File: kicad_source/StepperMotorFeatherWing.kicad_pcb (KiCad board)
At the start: 2 copper layers, 100 x 60 mm, 118 parts, among them CN1 ADAFRUIT_FEATHER, CN10 691322310004, CN11 BM05B-SRSS-TB, CN2 DNI, CN20 691322310004, CN21 BM05B-SRSS-TB, CN3 BM04B-SRSS-TB, CN4 CONN_01X04, CN5 691322310002, CN6 691313710002, Q1 IPD90P03P4L- 04, U1 TMC5130A-TA, U2 TMC5130A-TA, U3 LM1085ISX-ADJ/NOPB, U4 LM75BD, U9 IFX91041EJV, Y1 ECS-3225MV-160-BN-TR

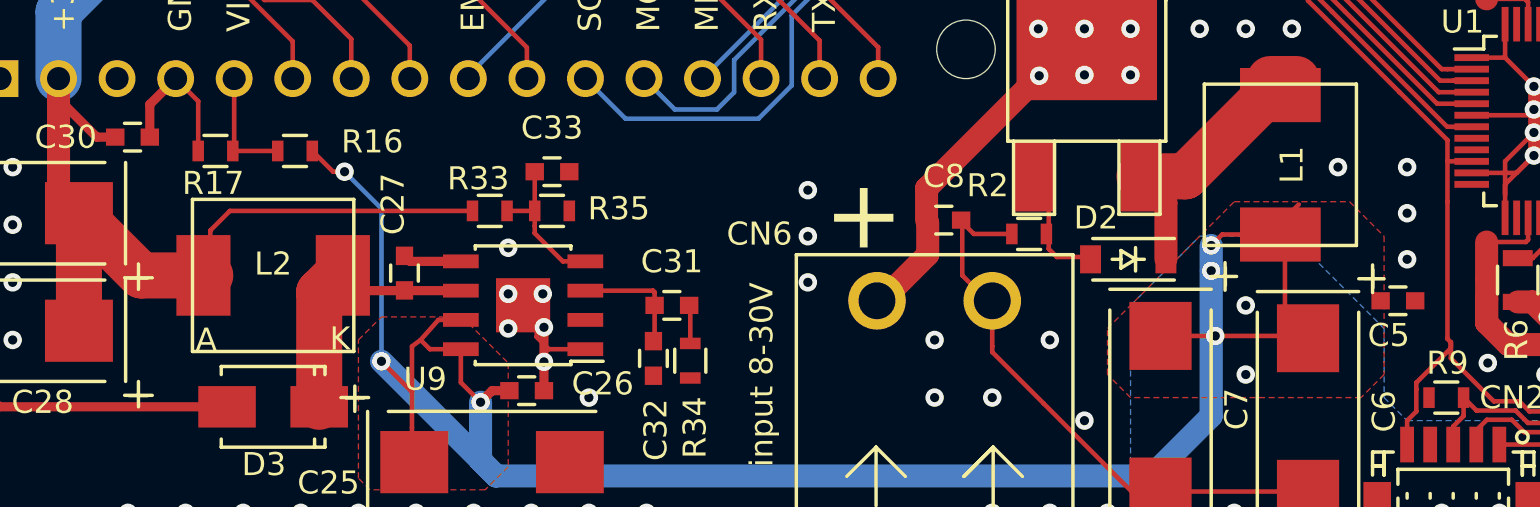
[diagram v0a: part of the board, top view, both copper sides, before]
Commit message: corrected order numbers of capacitors
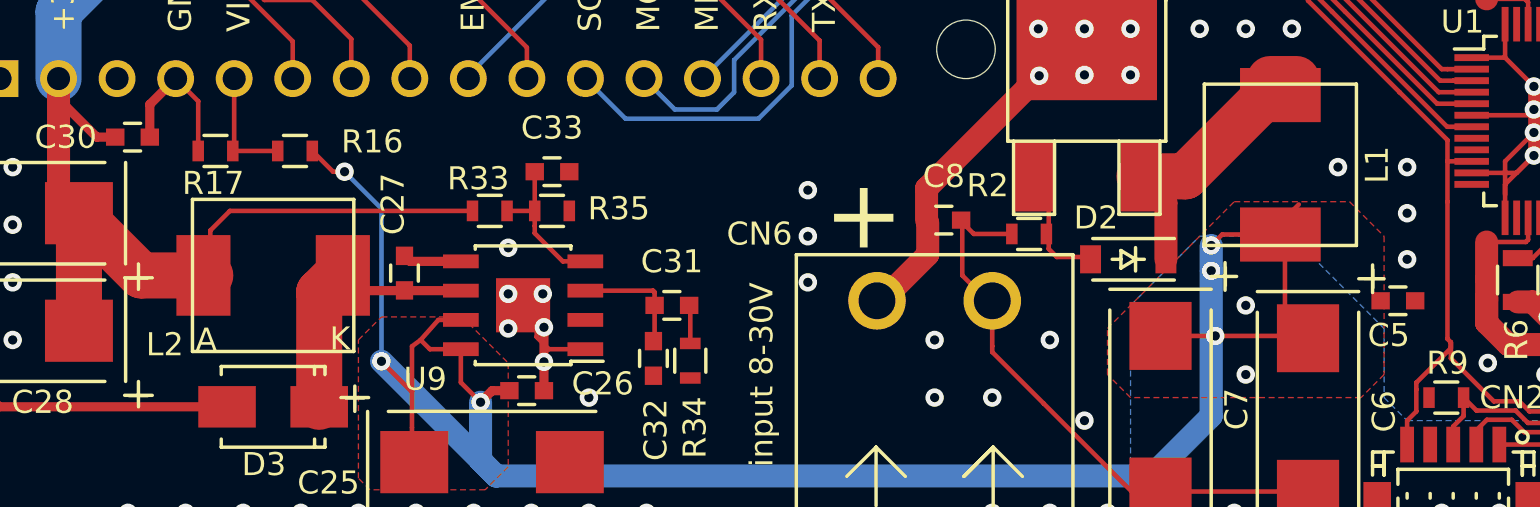
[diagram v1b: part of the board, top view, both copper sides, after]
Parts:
- C2, C3, C4: value 1000uF/50V -> DNI
- C25, C6, C7: value 47uF/50V -> T55D226M035C0120
- C28, C29: value 220uF/6V3 -> TCJY227M006R0050E

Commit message: updated pdf files
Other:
- board text added: "A"
- board text added: "B"
- board text added: "I2C Qwiic"
- board text added: "SPI option"
- board text removed: "Qwiic I2C"
